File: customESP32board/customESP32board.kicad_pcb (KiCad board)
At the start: 2 copper layers, 80 x 75 mm, 46 parts, among them J1 USB_B_Micro, J2 Conn_01x16_Pin, J3 Conn_01x16_Pin, Q1 S8050, Q2 S8050, Q3 BSS138, Q4 BSS138, Q5 BSS138, SW1 SW_Push, SW2 SW_Push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

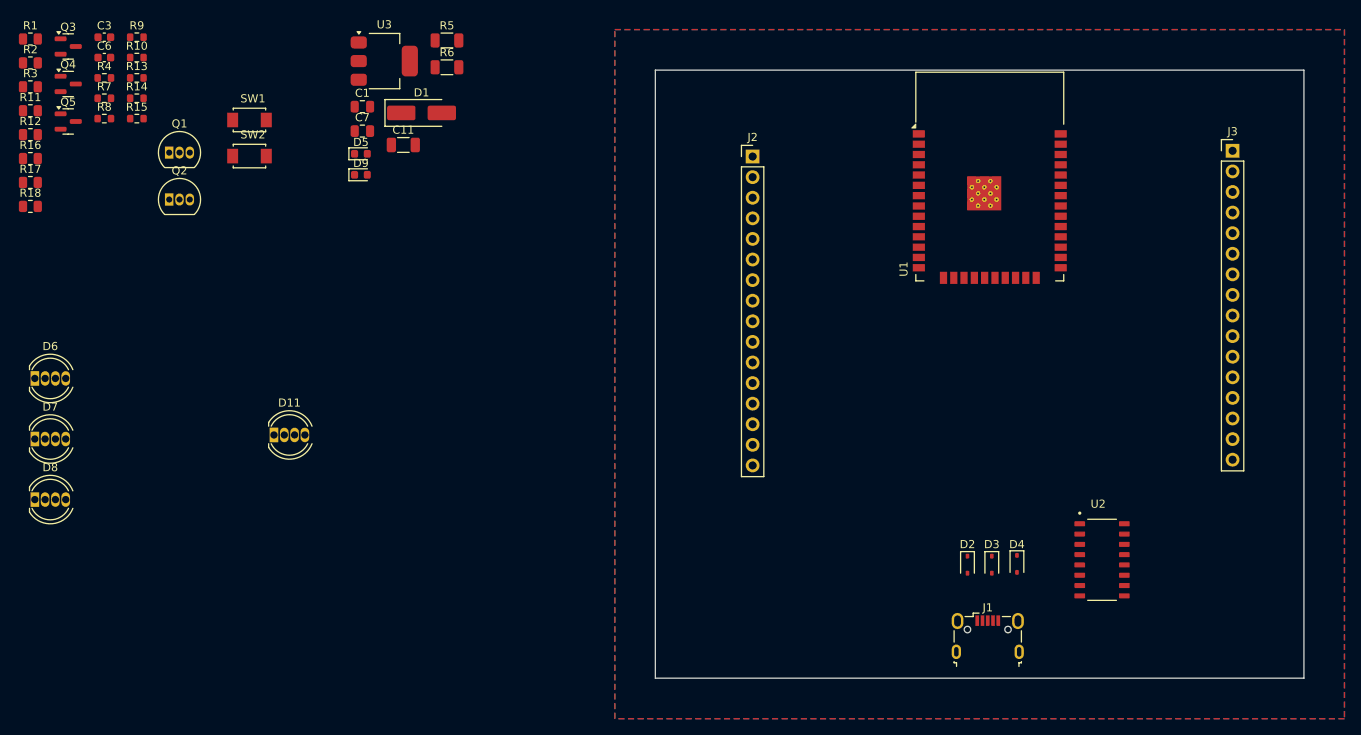
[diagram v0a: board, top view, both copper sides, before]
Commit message: continued layout, removed tvs diodes
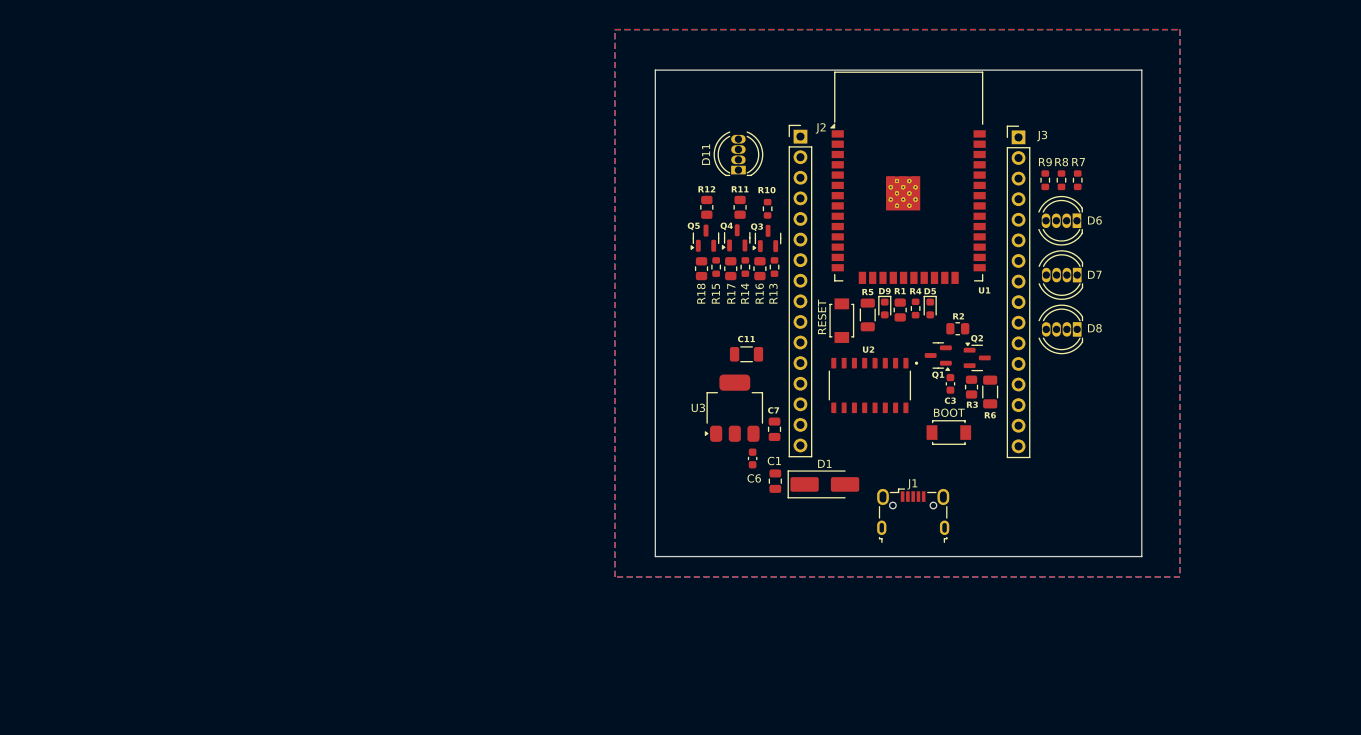
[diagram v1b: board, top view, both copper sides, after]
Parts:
- removed D2, D3, D4: SD05_SOD323, Diode_SMD:D_SOD-323
- removed SW1, SW2: SW_Push, TS-1088-AR02016:SW_TS-1088-AR02016
- added BOOT: SW_Push, TS-1088-AR02016:SW_TS-1088-AR02016, F.Cu at (140.7, 118.2)
- added RESET: SW_Push, TS-1088-AR02016:SW_TS-1088-AR02016, F.Cu at (127.5, 104.4)
- Q1, Q2: footprint Package_TO_SOT_THT:TO-92_Inline -> Package_TO_SOT_SMD:SOT-23
- moved D8 130.3 mm to (156.5, 105.5), turned to 180 degrees
- moved D7 130.2 mm to (156.5, 98.8), turned to 180 degrees
- moved D6 130.0 mm to (156.5, 92.1), turned to 180 degrees
- moved R3 121.9 mm to (143.5, 112.6), turned to 90 degrees
- moved R7 120.5 mm to (156.6, 87.1), turned to -90 degrees
- moved R2 119.0 mm to (141.8, 105.4), turned to 180 degrees
- moved R8 118.3 mm to (154.6, 87.1), turned to -90 degrees
- moved R9 113.4 mm to (152.6, 87.1), turned to -90 degrees
- moved C3 112.8 mm to (140.9, 112.2), turned to -90 degrees
- moved R1 112.4 mm to (134.7, 103.1), turned to 90 degrees
- moved R4 104.0 mm to (136.6, 102.9), turned to 90 degrees
- moved Q2 101.6 mm to (144.2, 109.0)
- moved Q1 98.1 mm to (139.4, 108.7), turned to 180 degrees
- moved C6 94.0 mm to (116.5, 121.4), turned to -90 degrees
- moved R16 91.0 mm to (117.4, 98.0), turned to -90 degrees
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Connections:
- R13 pad 2: ESP_IO22 -> ESP_IO25
- R14 pad 2: ESP_IO23 -> ESP_IO26
- R15 pad 2: ESP_IO25 -> ESP_IO27
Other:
- board size 80 x 75 mm -> 60 x 60 mm

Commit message: finished routing
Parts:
- removed BOOT, RESET: SW_Push, TS-1088-AR02016:SW_TS-1088-AR02016
- added SW1: SW_Push, TS-1088-AR02016:SW_TS-1088-AR02016, F.Cu at (124.6, 120.2)
- added SW2: SW_Push, TS-1088-AR02016:SW_TS-1088-AR02016, F.Cu at (144.9, 115.8)
- moved C1 24.6 mm to (143.9, 123.0), turned to 90 degrees
- moved C6 23.8 mm to (139.5, 115.2), turned to 0 degrees
- moved R1 23.2 mm to (114.4, 114.4), turned to 0 degrees
- moved D9 20.8 mm to (114.3, 112.4), turned to 180 degrees
- moved C7 20.5 mm to (139.7, 117.1), turned to 0 degrees
- moved U3 20.0 mm to (134.3, 116.1)
- moved R2 16.2 mm to (126.9, 111.7)
- moved D1 15.7 mm to (141.0, 122.9), turned to -90 degrees
- moved C11 15.5 mm to (129.4, 115.8), turned to -90 degrees
- moved C3 15.2 mm to (127.6, 104.8), turned to 180 degrees
- moved R5 13.1 mm to (125.0, 115.5), turned to 0 degrees
- moved Q1 11.8 mm to (127.6, 108.6), turned to -90 degrees
- moved R9 11.0 mm to (152.1, 98.1)
- moved R7 11.0 mm to (156.9, 98.1)
- moved D6 11.0 mm to (156.4, 103.1)
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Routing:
- net +3V3: track 0.00 -> 104.7 mm, vias 0 -> 5
- net +5V: track 0.00 -> 92.9 mm
- net ESP_EN: track 0.00 -> 49.4 mm, vias 0 -> 2
- net ESP_IO0: track 0.00 -> 35.1 mm
- net ESP_U0TX: track 0.00 -> 32.7 mm, vias 0 -> 2
- net ESP_U0RX: track 0.00 -> 30.8 mm, vias 0 -> 2
- net ESP_IO27: track 0.00 -> 26.8 mm
- net ESP_IO15: track 0.00 -> 23.6 mm, vias 0 -> 2
- net DTR: track 0.00 -> 21.0 mm, vias 0 -> 2
- net ESP_IO26: track 0.00 -> 19.5 mm
- net UD-: track 0.00 -> 18.9 mm, vias 0 -> 2
- net ESP_IO21: track 0.00 -> 18.8 mm
- net ESP_IO2: track 0.00 -> 18.7 mm, vias 0 -> 2
- net UD+: track 0.00 -> 18.5 mm, vias 0 -> 2
- net RGB_BLUE: track 0.00 -> 18.2 mm
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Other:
- board size 60 x 60 mm -> 55 x 55 mm
